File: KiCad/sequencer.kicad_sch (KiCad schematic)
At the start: 31 parts, among them J1 GATE OUT, J2 CLOCK IN, J5 RESET, J6 CV OUT, J7 CLOCK OUT, Q1 BC548, SW10 SW_Nidec_CAS-120A1, U1 TL074

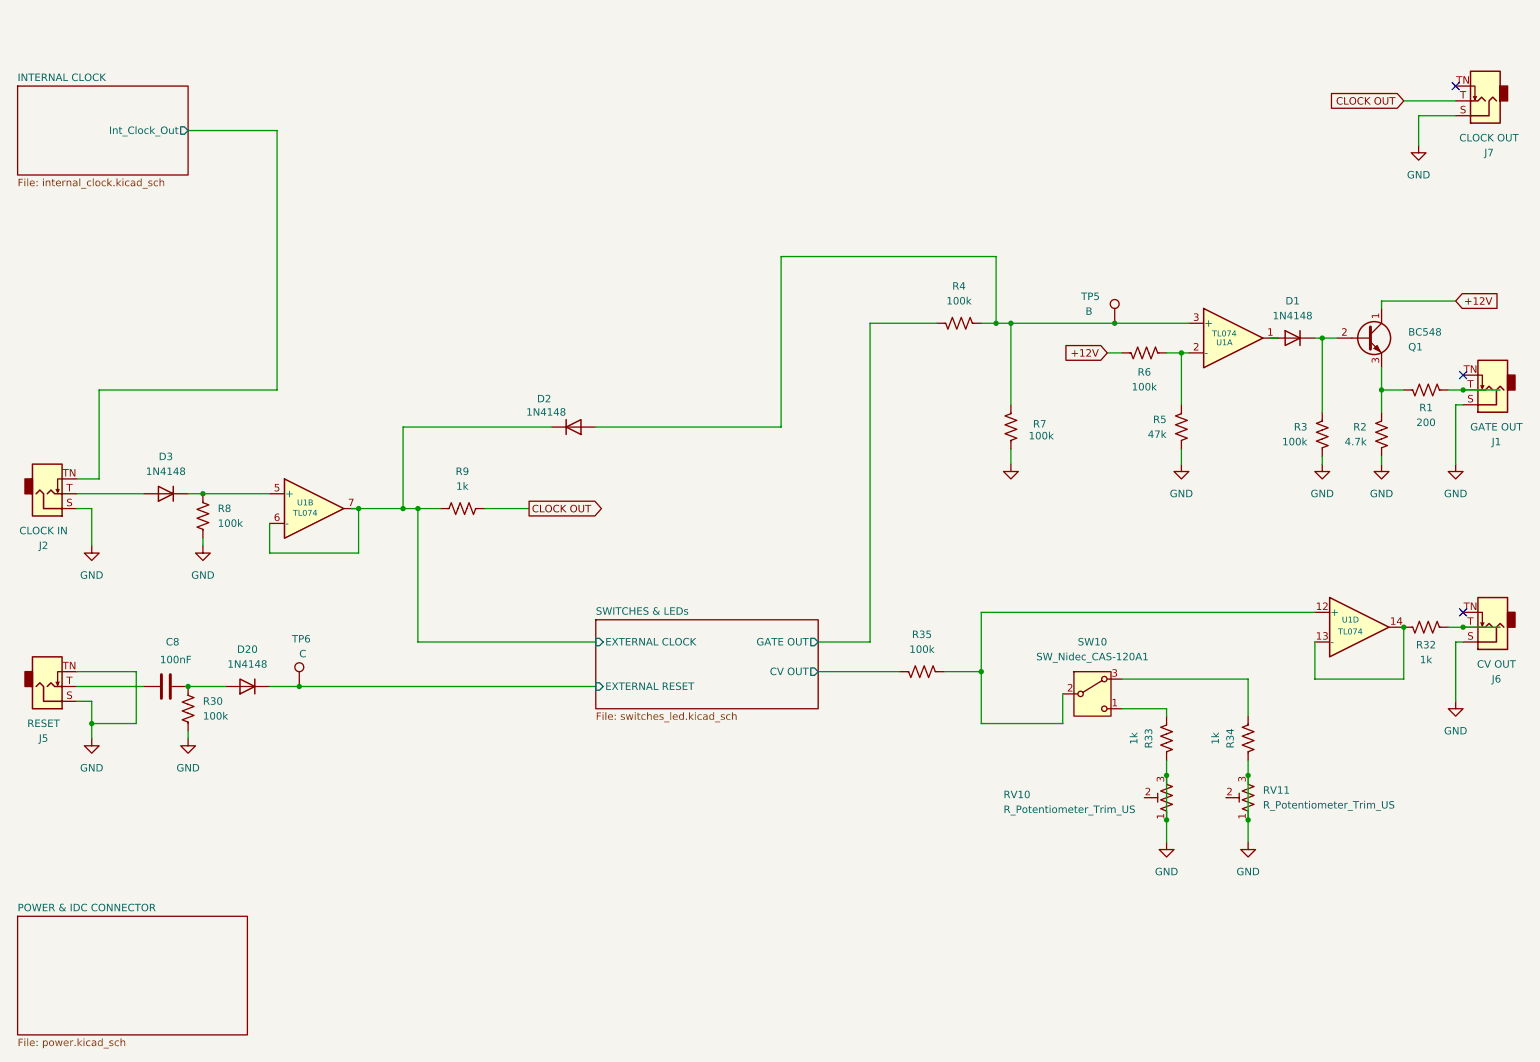
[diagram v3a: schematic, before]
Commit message: refactor(kicad): first ERC run
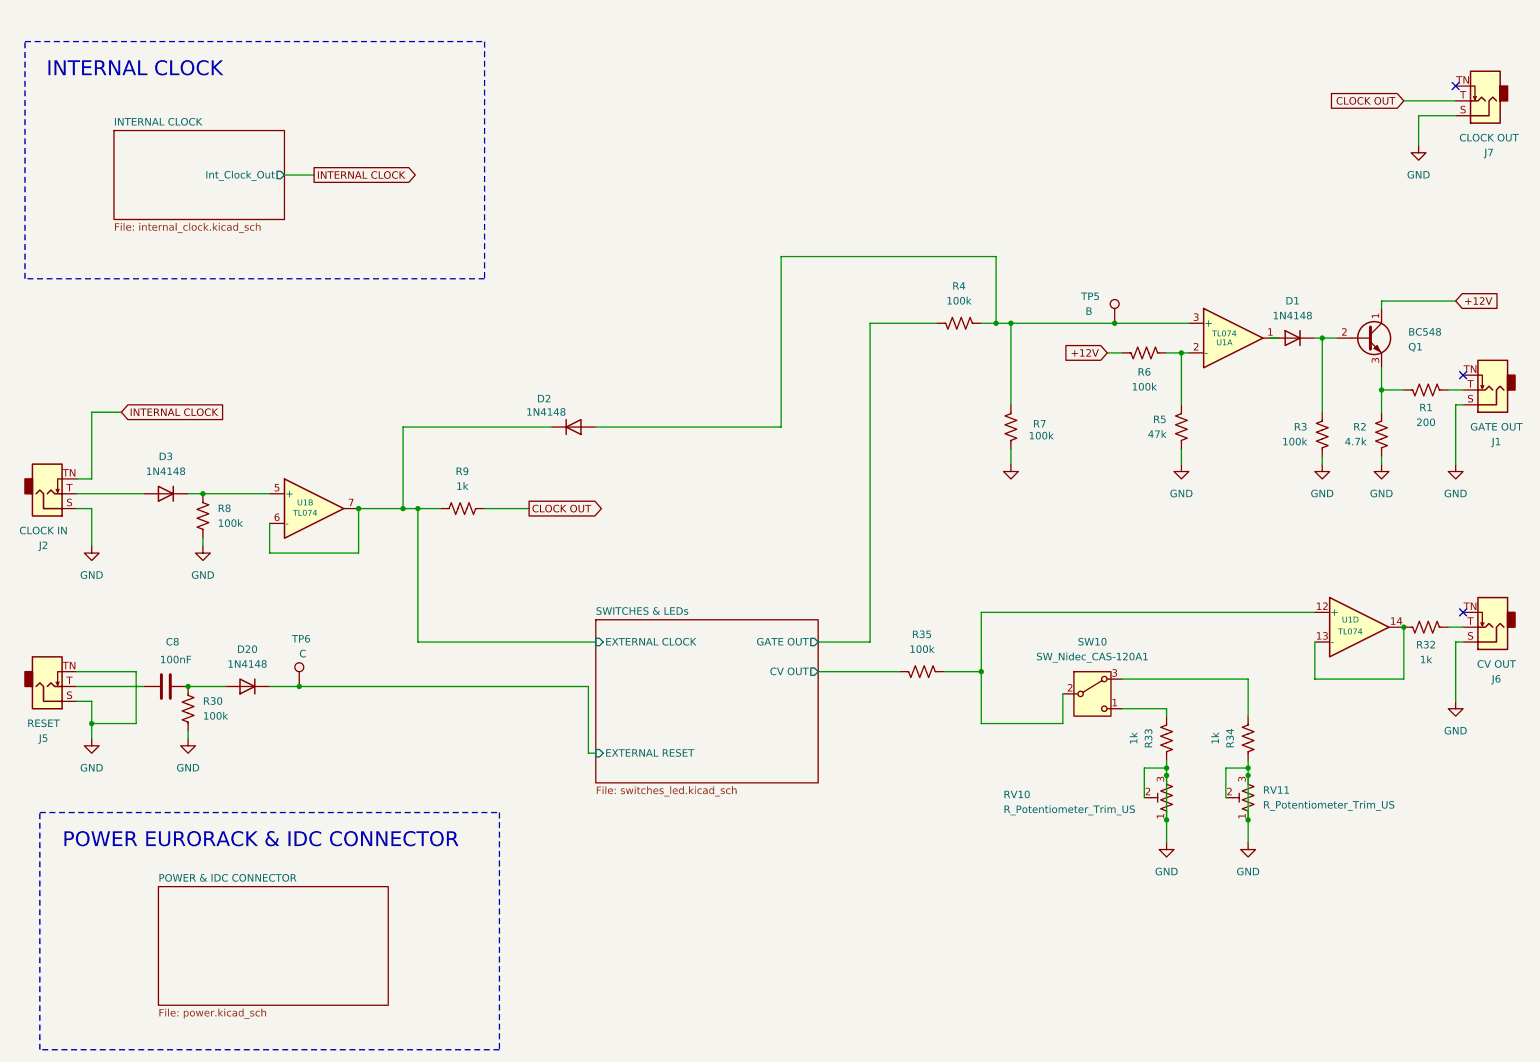
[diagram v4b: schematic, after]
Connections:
- net GND: now also RV10.2, RV11.2
- net INTERNAL CLOCK/Int_Clock_Out renamed INTERNAL CLOCK
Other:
- note added: "INTERNAL CLOCK"
- note added: "POWER EURORACK & IDC CONNECTOR"
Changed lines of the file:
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@@
 		(company "Dirty Dream - Nathanael Noir")
 	)
+	(rectangle
+		(start 20.32 20.32)
+		(end 99.06 60.96)
+		(stroke
+			(width 0)
+			(type dash)
+		)
+		(fill
+			(type none)
+		)
+	)
+	(rectangle
+		(start 22.86 152.4)
+		(end 101.6 193.04)
+		(stroke
+			(width 0)
+			(type dash)
+		)
+		(fill
+			(type none)
+		)
+	)
+	(text "POWER EURORACK & IDC CONNECTOR\n"
+		(exclude_from_sim no)
+		(at 60.706 157.226 0)
+		(effects
+			(font
+				(size 2.54 2.54)
+			)
+		)
+	)
+	(text "INTERNAL CLOCK"
+		(exclude_from_sim no)
+		(at 39.116 25.146 0)
+		(effects
+			(font
+				(size 2.54 2.54)
+			)
+		)
+	)
+	(junction
+		(at 215.9 144.78)
+		(diameter 0)
+		(color 0 0 0 0)
+	)
+	(junction
+		(at 229.87 144.78)
+		(diameter 0)
+		(color 0 0 0 0)
+	)
 	(junction
 		(at 85.09 100.33)
@@
 	)
 	(junction
-		(at 266.7 120.65)
-		(diameter 0)
-		(color 0 0 0 0)
-	)
-	(junction
 		(at 31.75 137.16)
 		(diameter 0)
@@
 	)
 	(junction
-		(at 266.7 80.01)
-		(diameter 0)
-		(color 0 0 0 0)
-	)
-	(junction
 		(at 218.44 73.66)
 		(diameter 0)
@@
 	(wire
 		(pts
-			(xy 215.9 143.51) (xy 215.9 146.05)
+			(xy 215.9 143.51) (xy 215.9 144.78)
 		)
 		(stroke
@@
 	(wire
 		(pts
-			(xy 266.7 120.65) (xy 264.16 120.65)
+			(xy 264.16 120.65) (xy 266.7 120.65)
 		)
 		(stroke
@@
 	(wire
 		(pts
+			(xy 116.84 142.24) (xy 116.84 130.81)
+		)
+		(stroke
+			(width 0)
+			(type default)
+		)
+	)
+	(wire
+		(pts
 			(xy 215.9 146.05) (xy 215.9 153.67)
 		)
@@
 	(wire
 		(pts
-			(xy 29.21 95.25) (xy 33.02 95.25)
+			(xy 31.75 95.25) (xy 29.21 95.25)
 		)
 		(stroke
@@
 	(wire
 		(pts
+			(xy 212.09 149.86) (xy 212.09 144.78)
+		)
+		(stroke
+			(width 0)
+			(type default)
+		)
+	)
+	(wire
+		(pts
 			(xy 189.23 90.17) (xy 189.23 92.71)
 		)
@@
 	(wire
 		(pts
+			(xy 226.06 149.86) (xy 226.06 144.78)
+		)
+		(stroke
+			(width 0)
+			(type default)
+		)
+	)
+	(wire
+		(pts
 			(xy 215.9 134.62) (xy 215.9 135.89)
 		)
@@
 	(wire
 		(pts
-			(xy 63.5 35.56) (xy 48.26 35.56)
+			(xy 69.85 43.18) (xy 64.77 43.18)
 		)
 		(stroke
@@
 	(wire
 		(pts
-			(xy 63.5 80.01) (xy 33.02 80.01)
+			(xy 36.83 83.82) (xy 31.75 83.82)
 		)
 		(stroke
@@
 	(wire
 		(pts
-			(xy 33.02 80.01) (xy 33.02 95.25)
+			(xy 31.75 83.82) (xy 31.75 95.25)
 		)
 		(stroke
@@
 	(wire
 		(pts
+			(xy 226.06 144.78) (xy 229.87 144.78)
+		)
+		(stroke
+			(width 0)
+			(type default)
+		)
+	)
+	(wire
+		(pts
+			(xy 229.87 144.78) (xy 229.87 146.05)
+		)
+		(stroke
+			(width 0)
+			(type default)
+		)
+	)
+	(wire
+		(pts
+			(xy 212.09 144.78) (xy 215.9 144.78)
+		)
+		(stroke
+			(width 0)
+			(type default)
+		)
+	)
+	(wire
+		(pts
 			(xy 252.73 91.44) (xy 252.73 92.71)
 		)
@@
 	(wire
 		(pts
-			(xy 67.31 130.81) (xy 118.11 130.81)
+			(xy 116.84 142.24) (xy 118.11 142.24)
 		)
 		(stroke
@@
 	(wire
 		(pts
-			(xy 229.87 143.51) (xy 229.87 146.05)
+			(xy 229.87 143.51) (xy 229.87 144.78)
 		)
 		(stroke
@@
 	(wire
 		(pts
-			(xy 266.7 80.01) (xy 264.16 80.01)
+			(xy 264.16 80.01) (xy 266.7 80.01)
 		)
 		(stroke
@@
 	(wire
 		(pts
-			(xy 63.5 35.56) (xy 63.5 80.01)
-		)
-		(stroke
-			(width 0)
-			(type default)
-		)
-	)
-	(wire
-		(pts
 			(xy 149.86 57.15) (xy 149.86 86.36)
 		)
@@
 	(wire
 		(pts
-			(xy 273.05 120.65) (xy 266.7 120.65)
-		)
-		(stroke
-			(width 0)
-			(type default)
-		)
-	)
-	(wire
-		(pts
 			(xy 118.11 86.36) (xy 149.86 86.36)
 		)
@@
 	(wire
 		(pts
-			(xy 76.2 100.33) (xy 77.47 100.33)
+			(xy 241.3 129.54) (xy 256.54 129.54)
 		)
 		(stroke
@@
 	(wire
 		(pts
-			(xy 241.3 129.54) (xy 256.54 129.54)
+			(xy 48.26 138.43) (xy 48.26 139.7)
 		)
 		(stroke
@@
 	(wire
 		(pts
-			(xy 48.26 138.43) (xy 48.26 139.7)
+			(xy 234.95 71.12) (xy 233.68 71.12)
 		)
 		(stroke
@@
 	(wire
 		(pts
-			(xy 234.95 71.12) (xy 233.68 71.12)
+			(xy 116.84 130.81) (xy 67.31 130.81)
 		)
 		(stroke
@@
 	(wire
 		(pts
-			(xy 273.05 80.01) (xy 266.7 80.01)
+			(xy 215.9 144.78) (xy 215.9 146.05)
 		)
 		(stroke
@@
 		)
 	)
+	(global_label "INTERNAL CLOCK"
+		(shape input)
+		(at 36.83 83.82 0)
+		(fields_autoplaced yes)
+		(effects
+			(font
+				(size 1.27 1.27)
+			)
+			(justify left)
+		)
+		(property "Intersheetrefs" "${INTERSHEET_REFS}"
+			(at 55.7205 83.82 0)
+			(effects
+				(font
+					(size 1.27 1.27)
+				)
+				(justify left)
+			)
+		)
+	)
+	(global_label "INTERNAL CLOCK"
+		(shape output)
+		(at 69.85 43.18 0)
+		(fields_autoplaced yes)
+		(effects
+			(font
+				(size 1.27 1.27)
+			)
+			(justify left)
+		)
+		(property "Intersheetrefs" "${INTERSHEET_REFS}"
+			(at 88.7405 43.18 0)
+			(effects
+				(font
+					(size 1.27 1.27)
+				)
+				(justify left)
+			)
+		)
+	)
 	(global_label "+12V"
 		(shape input)
@@
 	)
 	(sheet
-		(at 19.05 170.18)
+		(at 43.18 165.1)
 		(size 39.37 20.32)
 		(exclude_from_sim no)
@@
 		)
 		(property "Sheetname" "POWER & IDC CONNECTOR"
-			(at 19.05 169.4684 0)
+			(at 43.18 164.3884 0)
 			(effects
 				(font
@@
 		)
 		(property "Sheetfile" "power.kicad_sch"
-			(at 19.05 191.0846 0)
+			(at 43.18 186.0046 0)
 			(effects
 				(font
@@
 	(sheet
 		(at 118.11 119.38)
-		(size 38.1 15.24)
+		(size 38.1 27.94)
 		(exclude_from_sim no)
 		(in_bom yes)
@@
 		)
 		(property "Sheetfile" "switches_led.kicad_sch"
-			(at 118.11 135.2046 0)
+			(at 118.11 147.9046 0)
 			(effects
 				(font
@@
 		)
 		(pin "EXTERNAL RESET" input
-			(at 118.11 130.81 180)
+			(at 118.11 142.24 180)
 			(effects
 				(font
@@
 	)
 	(sheet
-		(at 19.05 27.94)
+		(at 35.56 35.56)
 		(size 29.21 15.24)
 		(exclude_from_sim no)
@@
 		)
 		(property "Sheetname" "INTERNAL CLOCK"
-			(at 19.05 27.2284 0)
+			(at 35.56 34.8484 0)
 			(effects
 				(font
@@
 		)
 		(property "Sheetfile" "internal_clock.kicad_sch"
-			(at 19.05 43.7646 0)
+			(at 35.56 51.3846 0)
 			(effects
 				(font
@@
 		)
 		(pin "Int_Clock_Out" output
-			(at 48.26 35.56 0)
+			(at 64.77 43.18 0)
 			(effects
 				(font

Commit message: Refine KiCad schematics for power, test points, and control values
  - replace schematic +12V/-12V global labels with proper power symbols
  - add GND test points and reorganize the power/IDC and main sequencer
  sheets
  - retune sequencer values including R33/R34 to 51k, R35 to 68k, C8 to
  1nF, and trim pots to 2k/5k
  - update switch/LED sheet labels and pot values, renaming LEDs by step
  and changing B250k controls to B100k
  - relax the KiCad four-way junction ERC setting in the project file
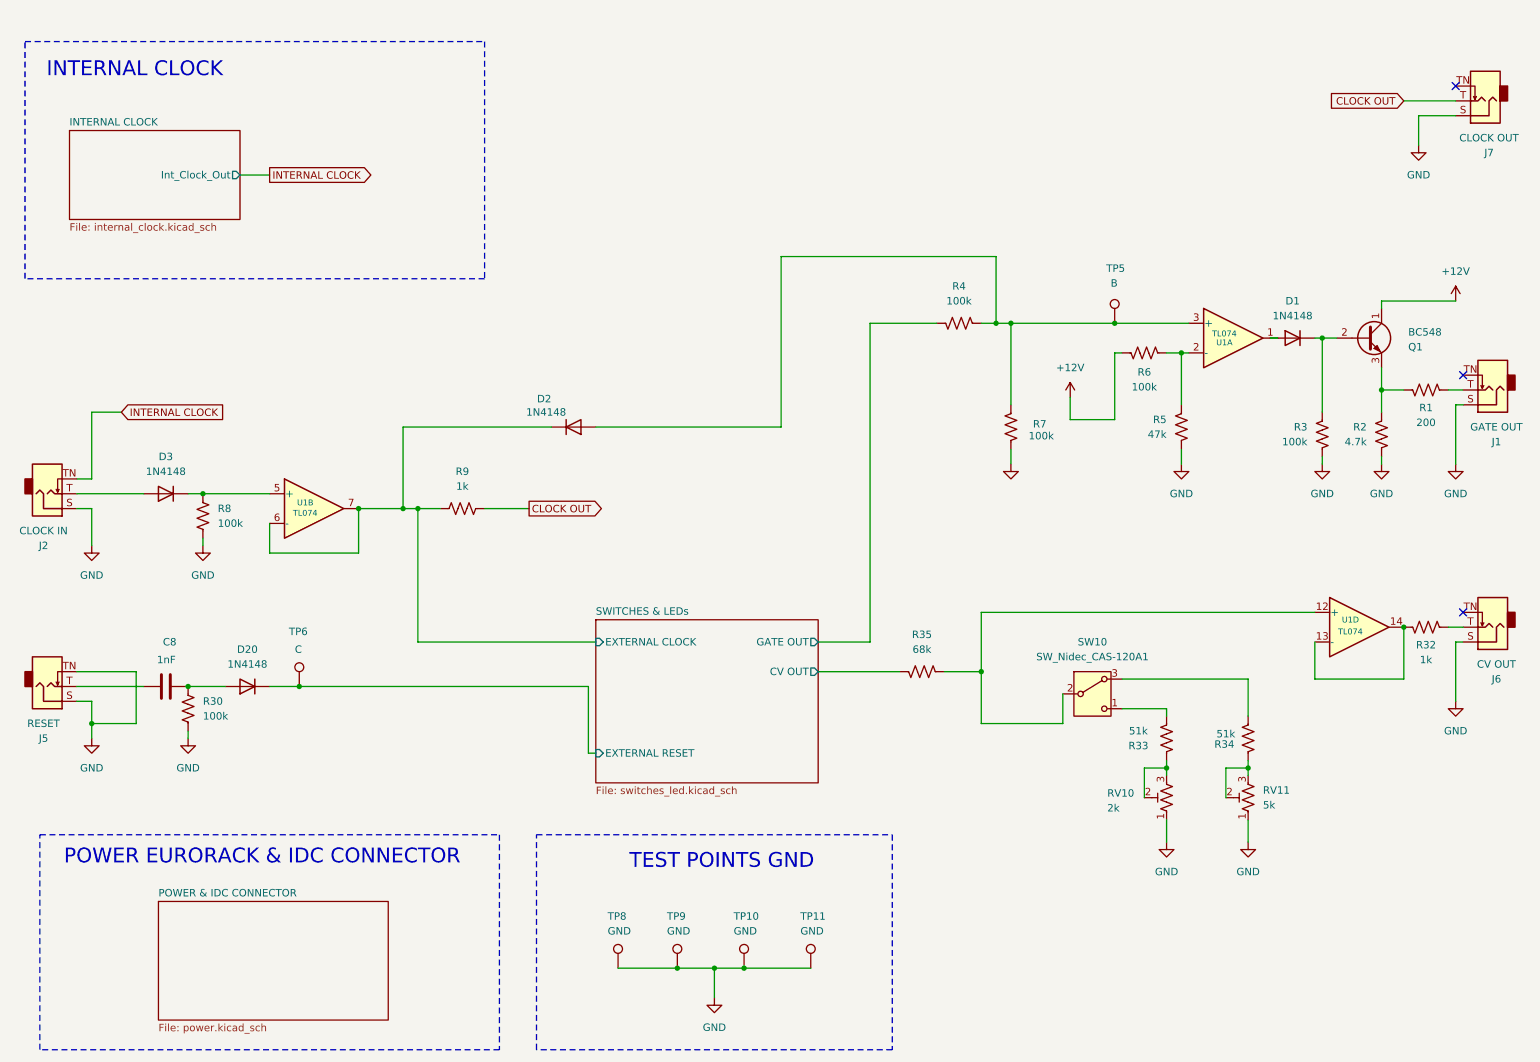
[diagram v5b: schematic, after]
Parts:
- added TP10, TP11, TP8, TP9: GND, symbol Connector:TestPoint
- C8: value 100nF -> 1nF
- R33, R34: value 1k -> 51k
- R35: value 100k -> 68k
- RV10: value R_Potentiometer_Trim_US -> 2k
- RV11: value R_Potentiometer_Trim_US -> 5k
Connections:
- net GND: now also TP10.1, TP11.1, TP8.1, TP9.1; no longer R33.1, R34.1, RV10.2, RV10.3, RV11.2, RV11.3
- new net: R33.1, RV10.2, RV10.3
- new net: R34.1, RV11.2, RV11.3
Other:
- note added: "TEST POINTS GND"
